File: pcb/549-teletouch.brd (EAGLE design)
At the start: 69.5 x 69.8 mm, 9 parts, among them IC1 MCP23017SP, IC2 MCP23017SP, J1 RASPBERRYPI-40-PIN-GPIO_PTH, J2 RASPBERRYPI-40-PIN-GPIO_PTH

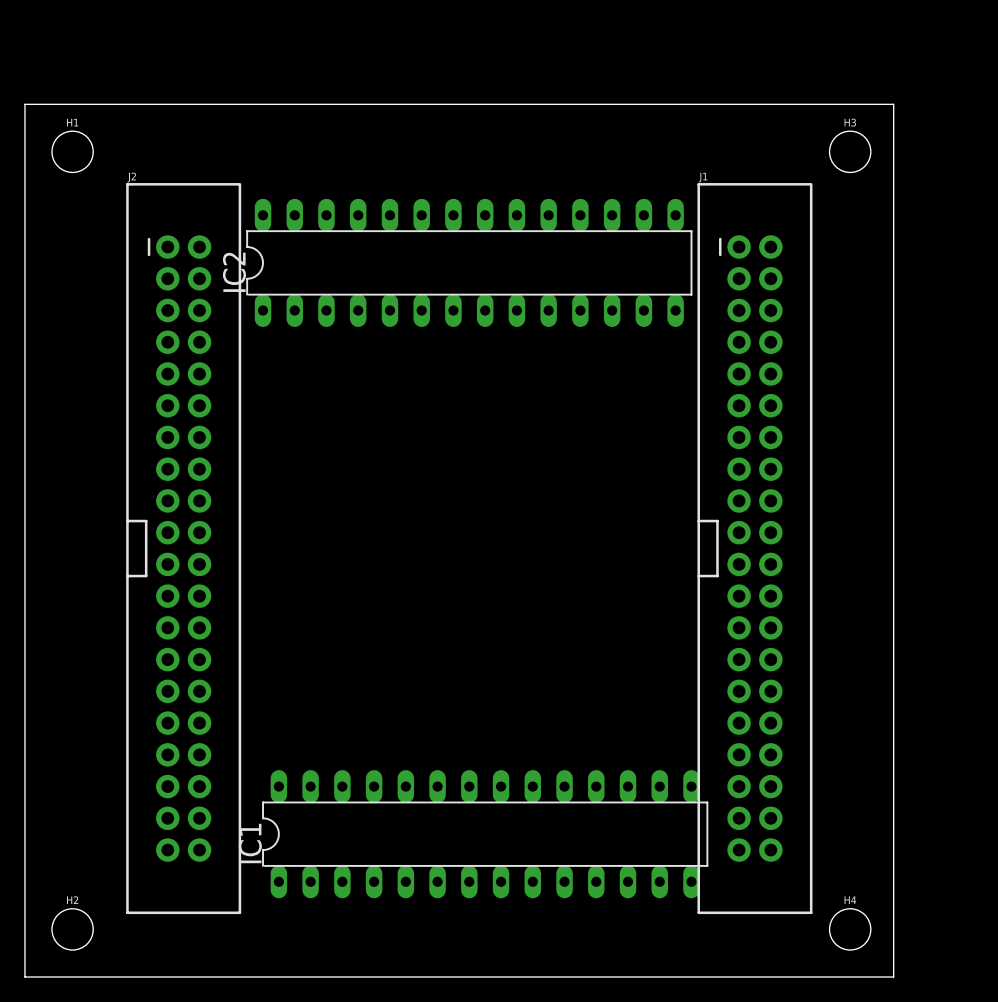
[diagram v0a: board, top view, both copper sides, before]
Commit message: Add auto-routed version.
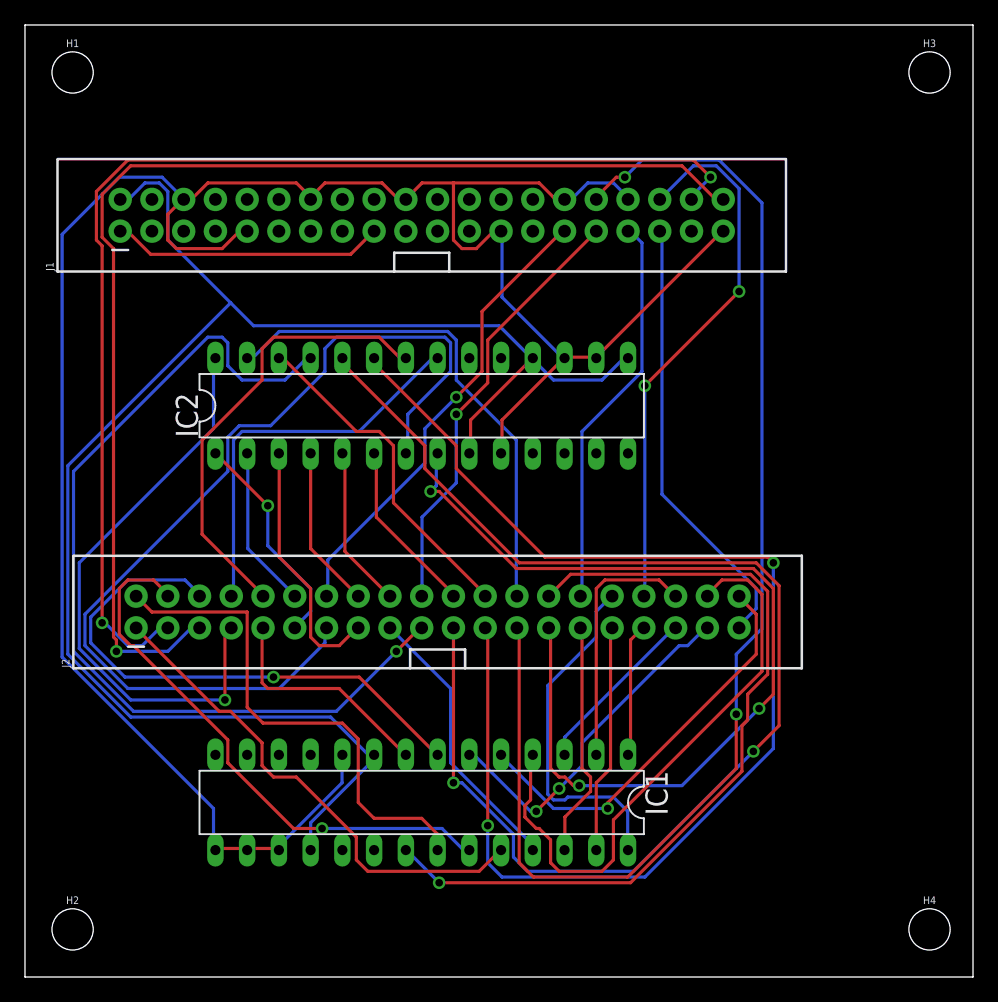
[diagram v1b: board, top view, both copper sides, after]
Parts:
- moved J1 37.7 mm to (31.8, 61.0), turned to 90 degrees
- moved J2 20.9 mm to (33.0, 29.2), turned to 90 degrees
- moved IC2 12.0 mm to (31.8, 45.7)
- moved H3 8.98 mm to (72.4, 72.4)
- moved H1 6.35 mm to (3.81, 72.4)
- moved H4 6.35 mm to (72.4, 3.81)
- moved IC1 5.68 mm to (31.8, 14.0), turned to 180 degrees
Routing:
- net GND: track 0.00 -> 181.5 mm
- net VDD: track 0.00 -> 131.8 mm
- net GP35: track 0.00 -> 102.6 mm, vias 0 -> 2
- net GP4: track 0.00 -> 102.3 mm, vias 0 -> 2
- net GP3: track 0.00 -> 101.5 mm, vias 0 -> 2
- net GP40: track 0.00 -> 96.3 mm, vias 0 -> 1
- net GP39: track 0.00 -> 94.6 mm, vias 0 -> 2
- net GP15: track 0.00 -> 77.6 mm
- net GP16: track 0.00 -> 75.2 mm, vias 0 -> 3
- net GP5: track 0.00 -> 73.7 mm, vias 0 -> 1
- net GP17: track 0.00 -> 65.7 mm, vias 0 -> 1
- net GP28: track 0.00 -> 47.2 mm
- net GP8: track 0.00 -> 47.1 mm, vias 0 -> 1
- net GP19: track 0.00 -> 44.7 mm, vias 0 -> 1
- net GP31: track 0.00 -> 44.1 mm, vias 0 -> 1
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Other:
- board size 69.5 x 69.8 mm -> 75.9 x 76.2 mm

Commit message: Update SDA / SCL connections in schematic and board.
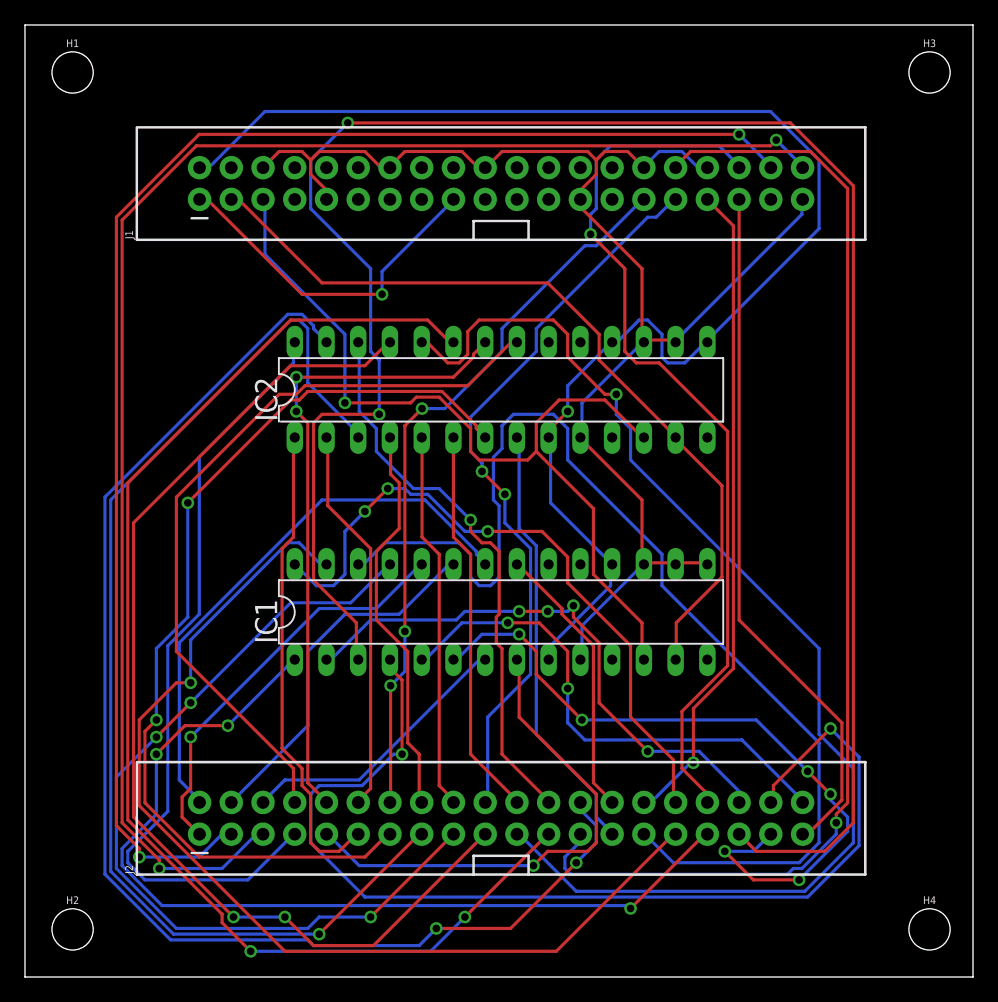
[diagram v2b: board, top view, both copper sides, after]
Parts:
- moved J2 17.3 mm to (38.1, 12.7)
- moved IC1 16.5 mm to (38.1, 29.2), turned to 0 degrees
- moved J1 6.84 mm to (38.1, 63.5)
- moved IC2 6.48 mm to (38.1, 47.0)
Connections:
- new net SCL: IC1.12, IC2.12, J1.5
- new net SDA: IC1.13, IC2.13, J1.3
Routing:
- net GP27: track 13.9 -> 157.0 mm, vias 0 -> 2
- net GP11: track 20.4 -> 92.5 mm, vias 0 -> 1
- net GP22: track 19.0 -> 90.6 mm
- net SCL: track 0.00 -> 71.1 mm, vias 0 -> 1
- net SDA: track 0.00 -> 65.6 mm
- net GP25: track 10.8 -> 75.0 mm, vias 0 -> 3
- net GND: track 181.5 -> 117.5 mm
- net GP23: track 18.3 -> 82.1 mm, vias 0 -> 1
- net GP7: track 40.4 -> 103.9 mm, vias 0 -> 2
- net GP21: track 22.5 -> 68.3 mm, vias 0 -> 3
- net GP17: track 65.7 -> 22.2 mm, vias 1 -> 0
- net GP16: track 75.2 -> 35.0 mm, vias 3 -> 0
- net GP28: track 47.2 -> 86.1 mm, vias 0 -> 2
- net GP30: track 28.1 -> 57.7 mm, vias 2 -> 6
- net GP1: track 31.6 -> 60.7 mm
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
